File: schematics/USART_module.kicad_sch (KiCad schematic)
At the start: 14 parts, among them J3 USB_B

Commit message: Файлы измененный Kicad
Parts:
- C0200: renamed from C200; footprint Capacitor_SMD:C_1206_3216Metric_Pad1.33x1.80mm_HandSolder -> Capacitor_SMD:C_0805_2012Metric
- C0201: renamed from C201; footprint Capacitor_SMD:C_1206_3216Metric_Pad1.33x1.80mm_HandSolder -> Capacitor_SMD:C_0805_2012Metric
- C0202: renamed from C202; footprint Capacitor_SMD:C_1206_3216Metric_Pad1.33x1.80mm_HandSolder -> Capacitor_SMD:C_0805_2012Metric
- C0203: renamed from C203; footprint Capacitor_SMD:C_1206_3216Metric_Pad1.33x1.80mm_HandSolder -> Capacitor_SMD:C_0805_2012Metric
- renumbered D2 to D0200, LD202 to LD0200, LD203 to LD0201, R200 to R0200, R201 to R0201, R202 to R0202, R203 to R0203, R204 to R0204, MK3 to U3
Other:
- moved on the sheet: C0201, C0202, C0203, R0200, R0201

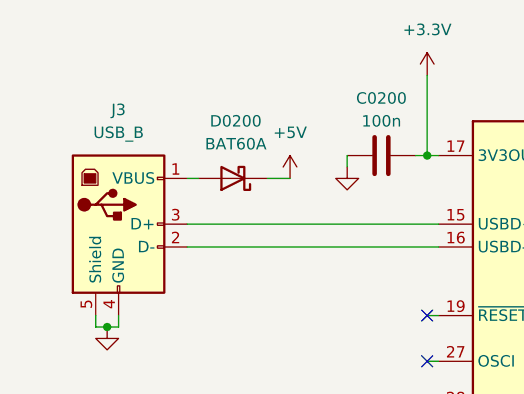
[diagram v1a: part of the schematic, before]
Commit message: Прошелся по всей схеме: 1. почистил компоненты; 2. задал посадочные места; 3. Выставил все ссылки на плате в притык, дальнейшее расширение - смена мк
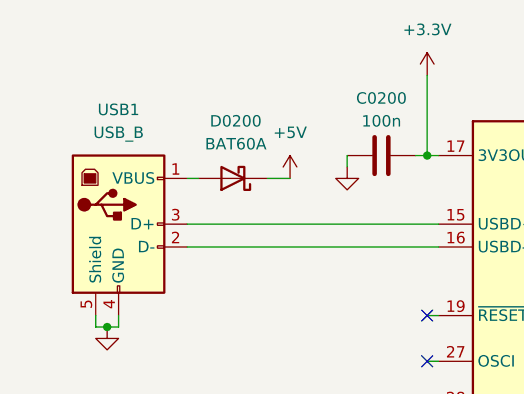
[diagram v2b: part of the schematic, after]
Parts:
- LD0200: value TX_YELLOW -> ~; footprint LED_SMD:LED_1206_3216Metric_Pad1.42x1.75mm_HandSolder -> LED_SMD:LED_0805_2012Metric
- LD0201: value RX_YELLOW -> ~; footprint LED_SMD:LED_1206_3216Metric_Pad1.42x1.75mm_HandSolder -> LED_SMD:LED_0805_2012Metric
- R0200, R0201, R0202, R0203, R0204: footprint Resistor_SMD:R_1206_3216Metric_Pad1.30x1.75mm_HandSolder -> Resistor_SMD:R_0805_2012Metric
- renumbered J3 to USB1
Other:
- company: (none) -> Филимонов и К
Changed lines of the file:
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@@
 	(title_block
 		(date "2025-02-23")
+		(company "Филимонов и К")
 		(comment 1 "RS232")
 		(comment 2 "Филимонов С.В.")
@@
 			)
 		)
-		(property "Value" "RX_YELLOW"
+		(property "Value" "~"
 			(at 203.2 102.87 0)
 			(effects
@@
 			)
 		)
-		(property "Footprint" "LED_SMD:LED_1206_3216Metric_Pad1.42x1.75mm_HandSolder"
+		(property "Footprint" "LED_SMD:LED_0805_2012Metric"
 			(at 194.31 104.14 0)
 			(effects
@@
 			)
 		)
-		(property "Footprint" "Resistor_SMD:R_1206_3216Metric_Pad1.30x1.75mm_HandSolder"
+		(property "Footprint" "Resistor_SMD:R_0805_2012Metric"
 			(at 207.01 105.918 90)
 			(effects
@@
 		(dnp no)
 		(fields_autoplaced yes)
-		(property "Reference" "J3"
+		(property "Reference" "USB1"
 			(at 104.14 71.12 0)
 			(effects
@@
 			(project "MasterBoard"
 				(path "/97e8f341-b455-4614-ab7f-cc310164e7aa/5af52d5a-2524-4f0f-872e-80f344338bdc"
-					(reference "J3")
+					(reference "USB1")
 					(unit 1)
 				)
@@
 			)
 		)
-		(property "Footprint" "Resistor_SMD:R_1206_3216Metric_Pad1.30x1.75mm_HandSolder"
+		(property "Footprint" "Resistor_SMD:R_0805_2012Metric"
 			(at 207.01 103.378 90)
 			(effects
@@
 			)
 		)
-		(property "Value" "TX_YELLOW"
+		(property "Value" "~"
 			(at 203.2 100.33 0)
 			(effects
@@
 			)
 		)
-		(property "Footprint" "LED_SMD:LED_1206_3216Metric_Pad1.42x1.75mm_HandSolder"
+		(property "Footprint" "LED_SMD:LED_0805_2012Metric"
 			(at 194.31 101.6 0)
 			(effects
@@
 			)
 		)
-		(property "Footprint" "Resistor_SMD:R_1206_3216Metric_Pad1.30x1.75mm_HandSolder"
+		(property "Footprint" "Resistor_SMD:R_0805_2012Metric"
 			(at 207.01 110.998 90)
 			(effects
@@
 			)
 		)
-		(property "Footprint" "Resistor_SMD:R_1206_3216Metric_Pad1.30x1.75mm_HandSolder"
+		(property "Footprint" "Resistor_SMD:R_0805_2012Metric"
 			(at 191.77 77.978 90)
 			(effects
@@
 			)
 		)
-		(property "Footprint" "Resistor_SMD:R_1206_3216Metric_Pad1.30x1.75mm_HandSolder"
+		(property "Footprint" "Resistor_SMD:R_0805_2012Metric"
 			(at 191.77 80.518 90)
 			(effects

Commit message: Множественные модификации
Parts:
- renumbered U3 to U2
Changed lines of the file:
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@@
 		(dnp no)
 		(fields_autoplaced yes)
-		(property "Reference" "U3"
+		(property "Reference" "U2"
 			(at 164.5159 68.58 0)
 			(effects
@@
 			(project "stm32f4_ILI_RS_SD"
 				(path "/97e8f341-b455-4614-ab7f-cc310164e7aa/5af52d5a-2524-4f0f-872e-80f344338bdc"
-					(reference "U3")
+					(reference "U2")
 					(unit 1)
 				)
